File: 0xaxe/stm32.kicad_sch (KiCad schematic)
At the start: 42 parts, among them J3 USB_C_Receptacle_USB2.0, J5 SWD, J6 Conn_01x05, M2 Fan_4pin, Q4 BSS138, SW1 boot, U3 STM32L072KZT6, U39 TXU0101, U5023 TMP1075, U89 TMP1075

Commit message: General Update
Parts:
- removed C165: 100n, Capacitor_SMD:C_0805_2012Metric, symbol Device:C
- removed J6: Conn_01x05, Connector_PinHeader_2.54mm:PinHeader_1x07_P2.54mm_Vertical, symbol Connector_Generic:Conn_01x07
- removed U89: TMP1075, myfootprints:TMP1075-DRL, symbol mylib7:TMP1075-DRL-SOT563
- added C10, C227: 311-3342-1-ND, Capacitor_SMD:C_0805_2012Metric, symbol Device:C
- added C8, C9: 1uF, Capacitor_SMD:C_0805_2012Metric, symbol Device:C
- added R106: 20k, Resistor_SMD:R_0805_2012Metric, symbol Device:R
- added U114: SN74AVC4T774, Package_SO:TSSOP-16_4.4x5mm_P0.65mm, symbol bitaxe:SN74AVC4T774
- added U91: MIC5504, Package_TO_SOT_SMD:SOT-23-5_HandSoldering, symbol bitaxe:MIC5504
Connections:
- net +3V3: now also C10.1, C8.1, U114.16 (VCCA), U91.1 (VIN), U91.3 (EN)
- net GND: now also C10.2, C227.1, C8.2, C9.2, R106.1, U114.1 (DIR1), U114.10 (GND), U91.2 (GND)
- net RESET: now also U114.12 (B3); no longer U3.18 (PA8)
- net RXD: now also U114.14 (B1); no longer U3.20 (PA10)
- net TXD: now also U114.13 (B2); no longer U3.19 (PA9)
- new net: R106.2, U114.9 (OE)
- new net 1V8_IO: C227.2, C9.1, U114.15 (VCCB), U114.2 (DIR2), U114.7 (DIR3), U91.5 (VOUT)
- new net STM_RST: U114.5 (A3), U3.18 (PA8)
- new net STM_RXD: U114.3 (A1), U3.20 (PA10)
- new net STM_TXD: U114.4 (A2), U3.19 (PA9)
- no-connect marks 11 -> 10
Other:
- note added: "1V8 LDO"
- note added: "300 mA max"
- note added: "Direction Control HIGH=A -> B LOW=A <- B"
- moved on the sheet: D5, D6, J3, J5, R27, R28, R30, R31, R36, R37

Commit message: fixed couple of things
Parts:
- removed C8, C9: 1uF, Capacitor_SMD:C_0805_2012Metric, symbol Device:C
- removed R106: 20k, Resistor_SMD:R_0805_2012Metric, symbol Device:R
- removed U91: MIC5504, Package_TO_SOT_SMD:SOT-23-5_HandSoldering, symbol bitaxe:MIC5504
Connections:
- net PWM_3V3_EXT is gone; now on net PWM_3V3: U3.11 (PA5)
- net GND: now also U114.11 (B4), U114.8 (DIR4), U114.9 (OE)
- net 1V8_IO renamed +1V8_3
- no-connect marks 10 -> 11
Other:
- note removed: "1V8 LDO"
- note removed: "300 mA max"
- moved on the sheet: C10, C227, C23, C5, C5056, C6, C9, D5, D6, J3, J5, M2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

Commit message: Layout update
Layout with OP
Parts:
- added J5: Conn_01x05, Connector_PinHeader_2.54mm:PinHeader_1x07_P2.54mm_Vertical, symbol Connector_Generic:Conn_01x07
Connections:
- net +1V8_3: now also U114.1 (DIR1); no longer U114.2 (DIR2)
- net +3V3: now also J5.1 (Pin_1)
- net GND: now also U114.2 (DIR2), J5.7 (Pin_7); no longer U114.1 (DIR1)
- net PWM_3V3: no longer U3.11 (PA5)
- net RESET: now also U114.14 (B1); no longer U114.12 (B3)
- net RXD: now also U114.13 (B2); no longer U114.14 (B1)
- net SCL: now also J5.5 (Pin_5)
- net SDA: now also J5.6 (Pin_6)
- net SPARE1: now also J5.3 (Pin_3)
- net SPARE2: now also J5.4 (Pin_4)
- net STM_RST: now also U114.3 (A1); no longer U114.5 (A3)
- net STM_RXD: now also U114.4 (A2); no longer U114.3 (A1)
- net STM_TXD: now also U114.5 (A3); no longer U114.4 (A2)
- net TXD: now also U114.12 (B3); no longer U114.13 (B2)
- new net PWM_3V3_EXT: J5.2 (Pin_2), U3.11 (PA5)

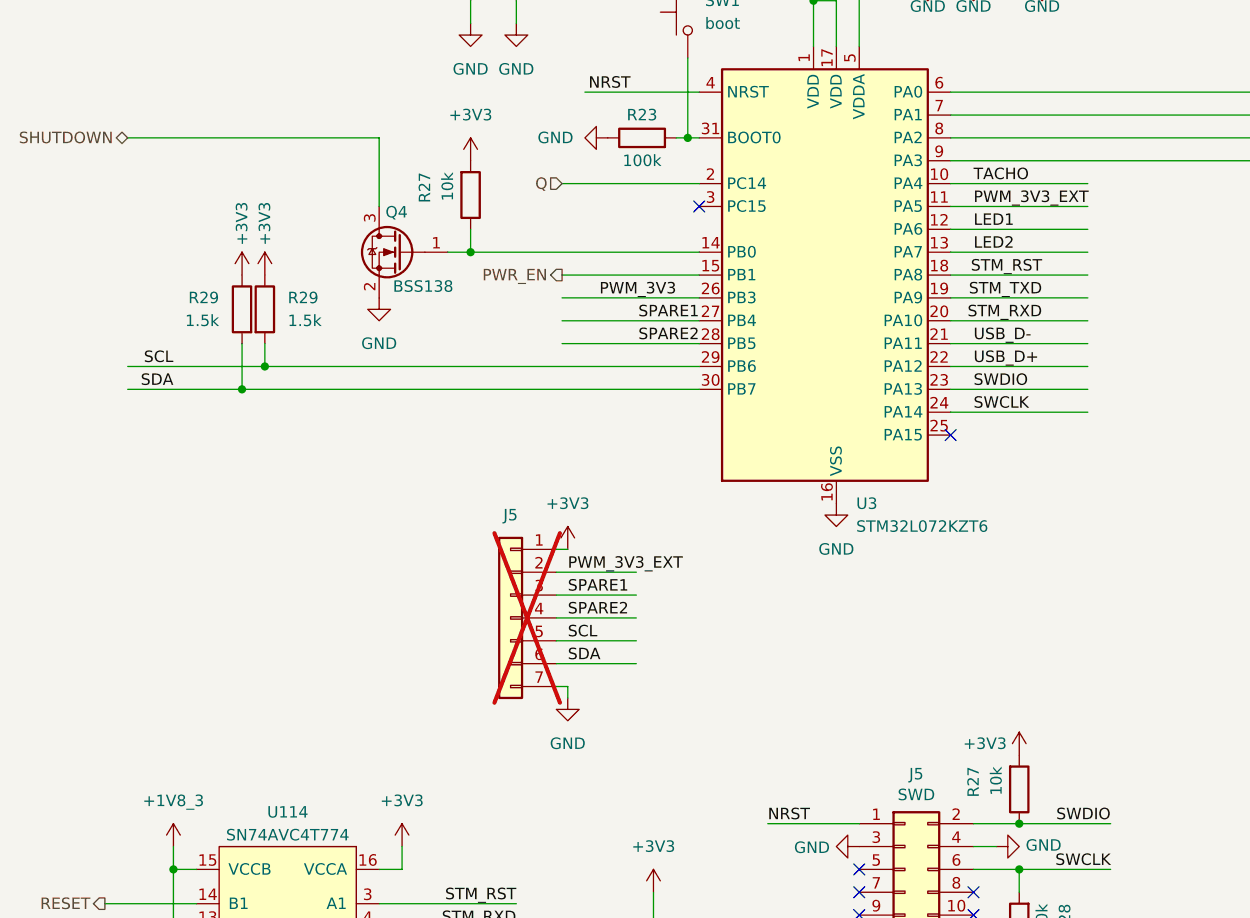
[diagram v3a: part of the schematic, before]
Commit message: fixed level shifter, added optional headers for future extensions
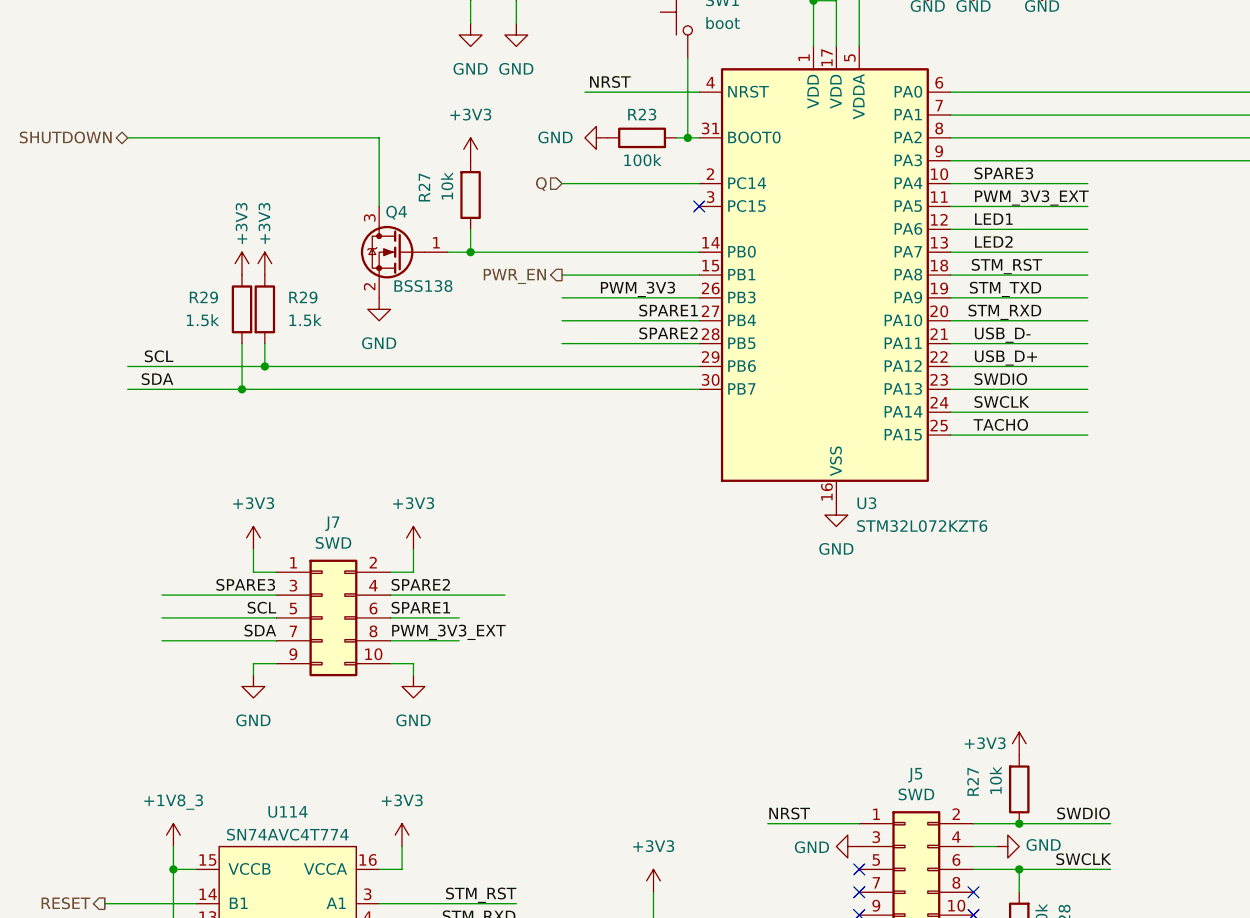
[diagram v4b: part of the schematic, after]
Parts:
- removed J5: Conn_01x05, Connector_PinHeader_2.54mm:PinHeader_1x07_P2.54mm_Vertical, symbol Connector_Generic:Conn_01x07
- added J7: SWD, myfootprints:PinHeader_IDC_2x05_P1.27mm_Vertical_SMD, symbol dwc-hat-rescue:Conn_02x05_Odd_Even-Connector_Generic
- C9: Distributor (none) -> D; Manufacturer (none) -> CAY16-1002F4LF; OrderNr (none) -> CAY16-1002F4LFCT-ND
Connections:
- net +3V3: now also J7.1 (Pin_1), J7.2 (Pin_2)
- net GND: now also J7.10 (Pin_10), J7.9 (Pin_9)
- net PWM_3V3_EXT: now also J7.8 (Pin_8)
- net SCL: now also J7.5 (Pin_5)
- net SDA: now also J7.7 (Pin_7)
- net SPARE1: now also J7.6 (Pin_6)
- net SPARE2: now also J7.4 (Pin_4)
- net TACHO: now also U3.25 (PA15); no longer U3.10 (PA4)
- new net SPARE3: J7.3 (Pin_3), U3.10 (PA4)
- no-connect marks 11 -> 10

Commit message: updated BOM and gerbers
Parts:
- C10, C227: value 311-3342-1-ND -> 100n
- U114: Distributor (none) -> D; Manufacturer (none) -> SN74AVC4T774PWR; OrderNr (none) -> 296-24739-1-ND
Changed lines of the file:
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@@
 			)
 		)
-		(property "Value" "311-3342-1-ND"
-			(at 38.1 163.83 0)
+		(property "Value" "100n"
+			(at 43.942 165.608 0)
 			(effects
 				(font
@@
 				)
 				(justify left bottom)
-				(hide yes)
 			)
 		)
@@
 			)
 		)
+		(property "Distributor" "D"
+			(at 73.66 161.29 0)
+			(effects
+				(font
+					(size 1.27 1.27)
+				)
+				(hide yes)
+			)
+		)
+		(property "Manufacturer" "SN74AVC4T774PWR"
+			(at 73.66 161.29 0)
+			(effects
+				(font
+					(size 1.27 1.27)
+				)
+				(hide yes)
+			)
+		)
+		(property "OrderNr" "296-24739-1-ND"
+			(at 73.66 161.29 0)
+			(effects
+				(font
+					(size 1.27 1.27)
+				)
+				(hide yes)
+			)
+		)
 		(pin "1"
 		)
@@
 			)
 		)
-		(property "Value" "311-3342-1-ND"
-			(at 114.3 163.83 0)
+		(property "Value" "100n"
+			(at 114.554 167.132 0)
 			(effects
 				(font
@@
 				)
 				(justify left bottom)
-				(hide yes)
-			)
-		)
+			)
+		)

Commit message: fixed BOM
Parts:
- C9: Distributor D -> (none); Manufacturer CAY16-1002F4LF -> (none); OrderNr CAY16-1002F4LFCT-ND -> (none)
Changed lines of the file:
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@@
 			)
 		)
-		(property "Distributor" "D"
+		(property "Distributor" ""
 			(at 157.48 46.99 0)
 			(effects
@@
 			)
 		)
-		(property "Manufacturer" "CAY16-1002F4LF"
+		(property "Manufacturer" ""
 			(at 157.48 46.99 0)
 			(effects
@@
 			)
 		)
-		(property "OrderNr" "CAY16-1002F4LFCT-ND"
+		(property "OrderNr" ""
 			(at 157.48 46.99 0)
 			(effects

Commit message: fixed bom
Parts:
- J7: now not fitted; now left out of the parts list
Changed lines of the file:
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@@
 		(unit 1)
 		(exclude_from_sim no)
-		(in_bom yes)
+		(in_bom no)
 		(on_board yes)
-		(dnp no)
+		(dnp yes)
 		(property "Reference" "J7"
 			(at 78.74 113.8682 0)
